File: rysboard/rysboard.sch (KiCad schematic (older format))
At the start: 1 part, among them J1 Raspberry_Pi_2_3

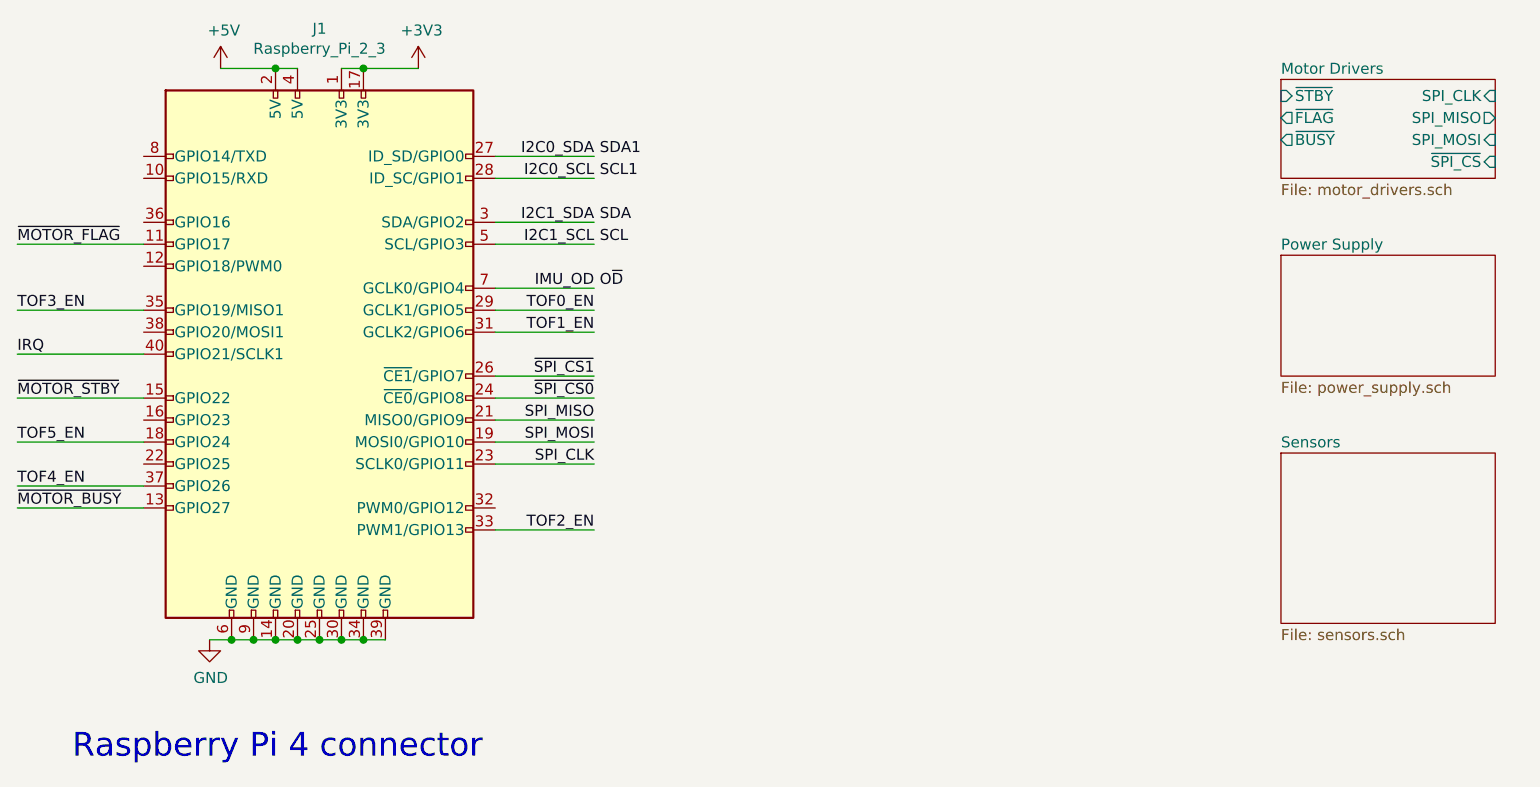
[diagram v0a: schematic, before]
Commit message: rysboard: schematic cleanup done after kicad import
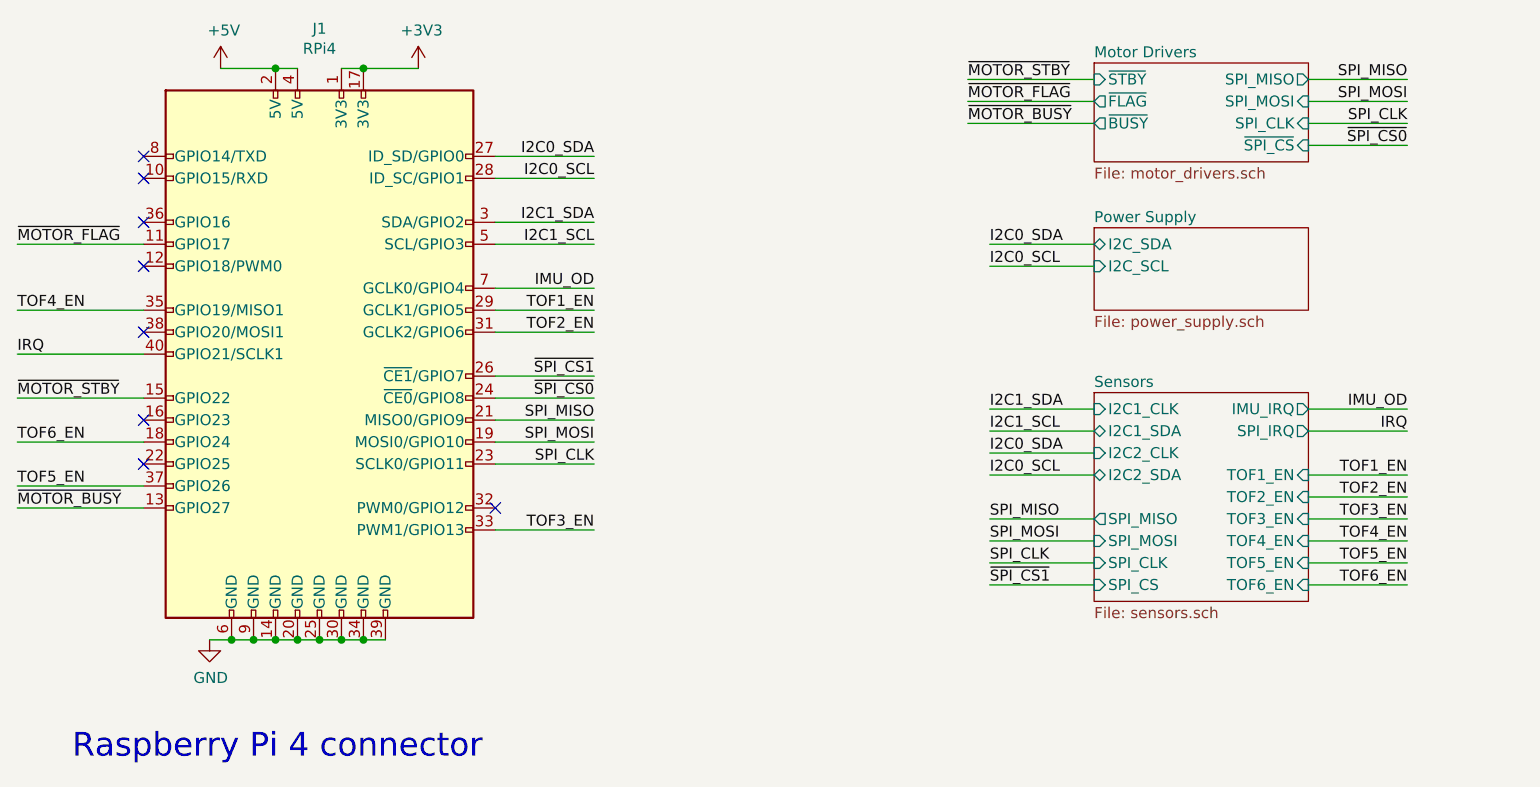
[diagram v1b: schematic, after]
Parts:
- J1: value Raspberry_Pi_2_3 -> RPi4; footprint (none) -> Connector_PinSocket_2.54mm:PinSocket_2x20_P2.54mm_Vertical
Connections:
- net TOF0_EN is gone; now on net TOF1_EN: J1.29 (GCLK1/GPIO5)
- net TOF1_EN: no longer J1.31 (GCLK2/GPIO6)
- net TOF2_EN: now also J1.31 (GCLK2/GPIO6); no longer J1.33 (PWM1/GPIO13)
- net TOF3_EN: now also J1.33 (PWM1/GPIO13); no longer J1.35 (GPIO19/MISO1)
- net TOF4_EN: now also J1.35 (GPIO19/MISO1); no longer J1.37 (GPIO26)
- net TOF5_EN: now also J1.37 (GPIO26); no longer J1.18 (GPIO24)
- new net TOF6_EN: J1.18 (GPIO24)
- no-connect marks 0 -> 8
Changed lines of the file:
@@
 Comment4 ""
 $EndDescr
-Text Label 4750 3025 0    50   ~ 0
-O~D~
-Text Label 4750 2525 0    50   ~ 0
-SCL1
-Text Label 4750 2425 0    50   ~ 0
-SDA1
 Text Notes 2350 5175 0    108  ~ 0
 Raspberry Pi 4 connector
-Text Label 4750 2825 0    50   ~ 0
-SCL
-Text Label 4750 2725 0    50   ~ 0
-SDA
 $Sheet
-S 7850 2075 975  450
+S 7000 2000 975  450
 U 5EB7428E
 F0 "Motor Drivers" 50
 F1 "motor_drivers.sch" 50
-F2 "~STBY" I L 7850 2150 50
-F3 "~FLAG" O L 7850 2250 50
-F4 "~BUSY" O L 7850 2350 50
-F5 "~SPI_CS" I R 8825 2450 50
-F6 "SPI_CLK" I R 8825 2150 50
-F7 "SPI_MISO" O R 8825 2250 50
-F8 "SPI_MOSI" I R 8825 2350 50
+F2 "~STBY" I L 7000 2075 50
+F3 "~FLAG" O L 7000 2175 50
+F4 "~BUSY" O L 7000 2275 50
+F5 "~SPI_CS" I R 7975 2375 50
+F6 "SPI_CLK" I R 7975 2275 50
+F7 "SPI_MISO" O R 7975 2075 50
+F8 "SPI_MOSI" I R 7975 2175 50
 $EndSheet
 $Sheet
-S 7850 2875 975  550
+S 7000 2750 975  375
 U 5E8FCBC6
 F0 "Power Supply" 50
 F1 "power_supply.sch" 50
+F2 "I2C_SDA" B L 7000 2825 50
+F3 "I2C_SCL" I L 7000 2925 50
 $EndSheet
 $Comp
@@
 P 3475 3325
 F 0 "J1" H 3475 4806 50  0000 C CNN
-F 1 "Raspberry_Pi_2_3" H 3475 4715 50  0000 C CNN
-F 2 "" H 3475 3325 50  0001 C CNN
+F 1 "RPi4" H 3475 4715 50  0000 C CNN
+F 2 "Connector_PinSocket_2.54mm:PinSocket_2x20_P2.54mm_Vertical" H 3475 3325 50  0001 C CNN
 F 3 "https://www.raspberrypi.org/documentation/hardware/raspberrypi/schematics/rpi_SCH_3bplus_1p0_reduced.pdf" H 3475 3325 50  0001 C CNN
 	1    3475 3325
@@
 $EndComp
 $Comp
-L power:+5V #PWR?
+L power:+5V #PWR02
 U 1 1 5EB8A55F
 P 3025 2025
-F 0 "#PWR?" H 3025 1875 50  0001 C CNN
+F 0 "#PWR02" H 3025 1875 50  0001 C CNN
 F 1 "+5V" H 3040 2198 50  0000 C CNN
 F 2 "" H 3025 2025 50  0001 C CNN
@@
 Connection ~ 3275 2025
 $Comp
-L power:+3V3 #PWR?
+L power:+3V3 #PWR03
 U 1 1 5EB8D8B6
 P 3925 2025
-F 0 "#PWR?" H 3925 1875 50  0001 C CNN
+F 0 "#PWR03" H 3925 1875 50  0001 C CNN
 F 1 "+3V3" H 3940 2198 50  0000 C CNN
 F 2 "" H 3925 2025 50  0001 C CNN
@@
 Connection ~ 3675 2025
 $Comp
-L power:GND #PWR?
+L power:GND #PWR01
 U 1 1 5EB9309D
 P 2975 4625
-F 0 "#PWR?" H 2975 4375 50  0001 C CNN
+F 0 "#PWR01" H 2975 4375 50  0001 C CNN
 F 1 "GND" H 2980 4452 50  0000 C CNN
 F 2 "" H 2975 4625 50  0001 C CNN
@@
 ~MOTOR_BUSY
 $Sheet
-S 7850 3775 975  775
+S 7000 3500 975  950
 U 5EA6D11C
 F0 "Sensors" 50
 F1 "sensors.sch" 50
+F2 "TOF6_EN" I R 7975 4375 50
+F3 "TOF5_EN" I R 7975 4275 50
+F4 "TOF4_EN" I R 7975 4175 50
+F5 "TOF2_EN" I R 7975 3975 50
+F6 "TOF1_EN" I R 7975 3875 50
+F7 "I2C1_CLK" I L 7000 3575 50
+F8 "I2C1_SDA" B L 7000 3675 50
+F9 "TOF3_EN" I R 7975 4075 50
+F10 "SPI_MOSI" I L 7000 4175 50
+F11 "SPI_MISO" O L 7000 4075 50
+F12 "SPI_CLK" I L 7000 4275 50
+F13 "SPI_CS" I L 7000 4375 50
+F14 "SPI_IRQ" O R 7975 3675 50
+F15 "I2C2_CLK" I L 7000 3775 50
+F16 "I2C2_SDA" B L 7000 3875 50
+F17 "IMU_IRQ" O R 7975 3575 50
 $EndSheet
 Wire Wire Line
@@
 	2675 3925 2100 3925
 Text Label 4725 3125 2    50   ~ 0
-TOF0_EN
+TOF1_EN
 Text Label 4725 3225 2    50   ~ 0
-TOF1_EN
+TOF2_EN
 Text Label 4725 4125 2    50   ~ 0
-TOF2_EN
+TOF3_EN
 Text Label 2100 3125 0    50   ~ 0
-TOF3_EN
+TOF4_EN
 Text Label 2100 3925 0    50   ~ 0
-TOF4_EN
+TOF5_EN
 Wire Wire Line
 	2675 3725 2100 3725
 Text Label 2100 3725 0    50   ~ 0
+TOF6_EN
+Wire Wire Line
+	7000 2175 6425 2175
+Text Label 6425 2175 0    50   ~ 0
+~MOTOR_FLAG
+Wire Wire Line
+	7000 2075 6425 2075
+Text Label 6425 2075 0    50   ~ 0
+~MOTOR_STBY
+Wire Wire Line
+	7000 2275 6425 2275
+Text Label 6425 2275 0    50   ~ 0
+~MOTOR_BUSY
+Wire Wire Line
+	7975 2075 8425 2075
+Text Label 8425 2075 2    50   ~ 0
+SPI_MISO
+Wire Wire Line
+	7975 2175 8425 2175
+Text Label 8425 2175 2    50   ~ 0
+SPI_MOSI
+Wire Wire Line
+	7975 2275 8425 2275
+Text Label 8425 2275 2    50   ~ 0
+SPI_CLK
+Wire Wire Line
+	7975 2375 8425 2375
+Text Label 8425 2375 2    50   ~ 0
+~SPI_CS0
+Text Label 6525 4075 0    50   ~ 0
+SPI_MISO
+Text Label 6525 4175 0    50   ~ 0
+SPI_MOSI
+Text Label 6525 4275 0    50   ~ 0
+SPI_CLK
+Text Label 6525 4375 0    50   ~ 0
+~SPI_CS1
+Wire Wire Line
+	7000 4075 6525 4075
+Wire Wire Line
+	6525 4175 7000 4175
+Wire Wire Line
+	7000 4275 6525 4275
+Wire Wire Line
+	6525 4375 7000 4375
+Text Label 6525 3875 0    50   ~ 0
+I2C0_SCL
+Text Label 6525 3775 0    50   ~ 0
+I2C0_SDA
+Text Label 6525 3575 0    50   ~ 0
+I2C1_SDA
+Text Label 6525 3675 0    50   ~ 0
+I2C1_SCL
+Wire Wire Line
+	7000 3575 6525 3575
+Wire Wire Line
+	6525 3675 7000 3675
+Wire Wire Line
+	7000 3775 6525 3775
+Wire Wire Line
+	6525 3875 7000 3875
+Text Label 6525 2925 0    50   ~ 0
+I2C0_SCL
+Text Label 6525 2825 0    50   ~ 0
+I2C0_SDA
+Wire Wire Line
+	7000 2825 6525 2825
+Wire Wire Line
+	6525 2925 7000 2925
+Wire Wire Line
+	7975 3875 8425 3875
+Wire Wire Line
+	7975 3975 8425 3975
+Text Label 8425 3875 2    50   ~ 0
+TOF1_EN
+Text Label 8425 3975 2    50   ~ 0
+TOF2_EN
+Wire Wire Line
+	7975 3575 8425 3575
+Text Label 8425 3575 2    50   ~ 0
+IMU_OD
+Text Label 8425 3675 2    50   ~ 0
+IRQ
+Wire Wire Line
+	7975 3675 8425 3675
+Wire Wire Line
+	7975 4075 8425 4075
+Text Label 8425 4075 2    50   ~ 0
+TOF3_EN
+Text Label 8425 4175 2    50   ~ 0
+TOF4_EN
+Text Label 8425 4275 2    50   ~ 0
 TOF5_EN
+Text Label 8425 4375 2    50   ~ 0
+TOF6_EN
+Wire Wire Line
+	7975 4175 8425 4175
+Wire Wire Line
+	7975 4275 8425 4275
+Wire Wire Line
+	7975 4375 8425 4375
+NoConn ~ 2675 2425
+NoConn ~ 2675 2525
+NoConn ~ 2675 2725
+NoConn ~ 2675 2925
+NoConn ~ 4275 4025
+NoConn ~ 2675 3825
+NoConn ~ 2675 3625
+NoConn ~ 2675 3225
 $EndSCHEMATC

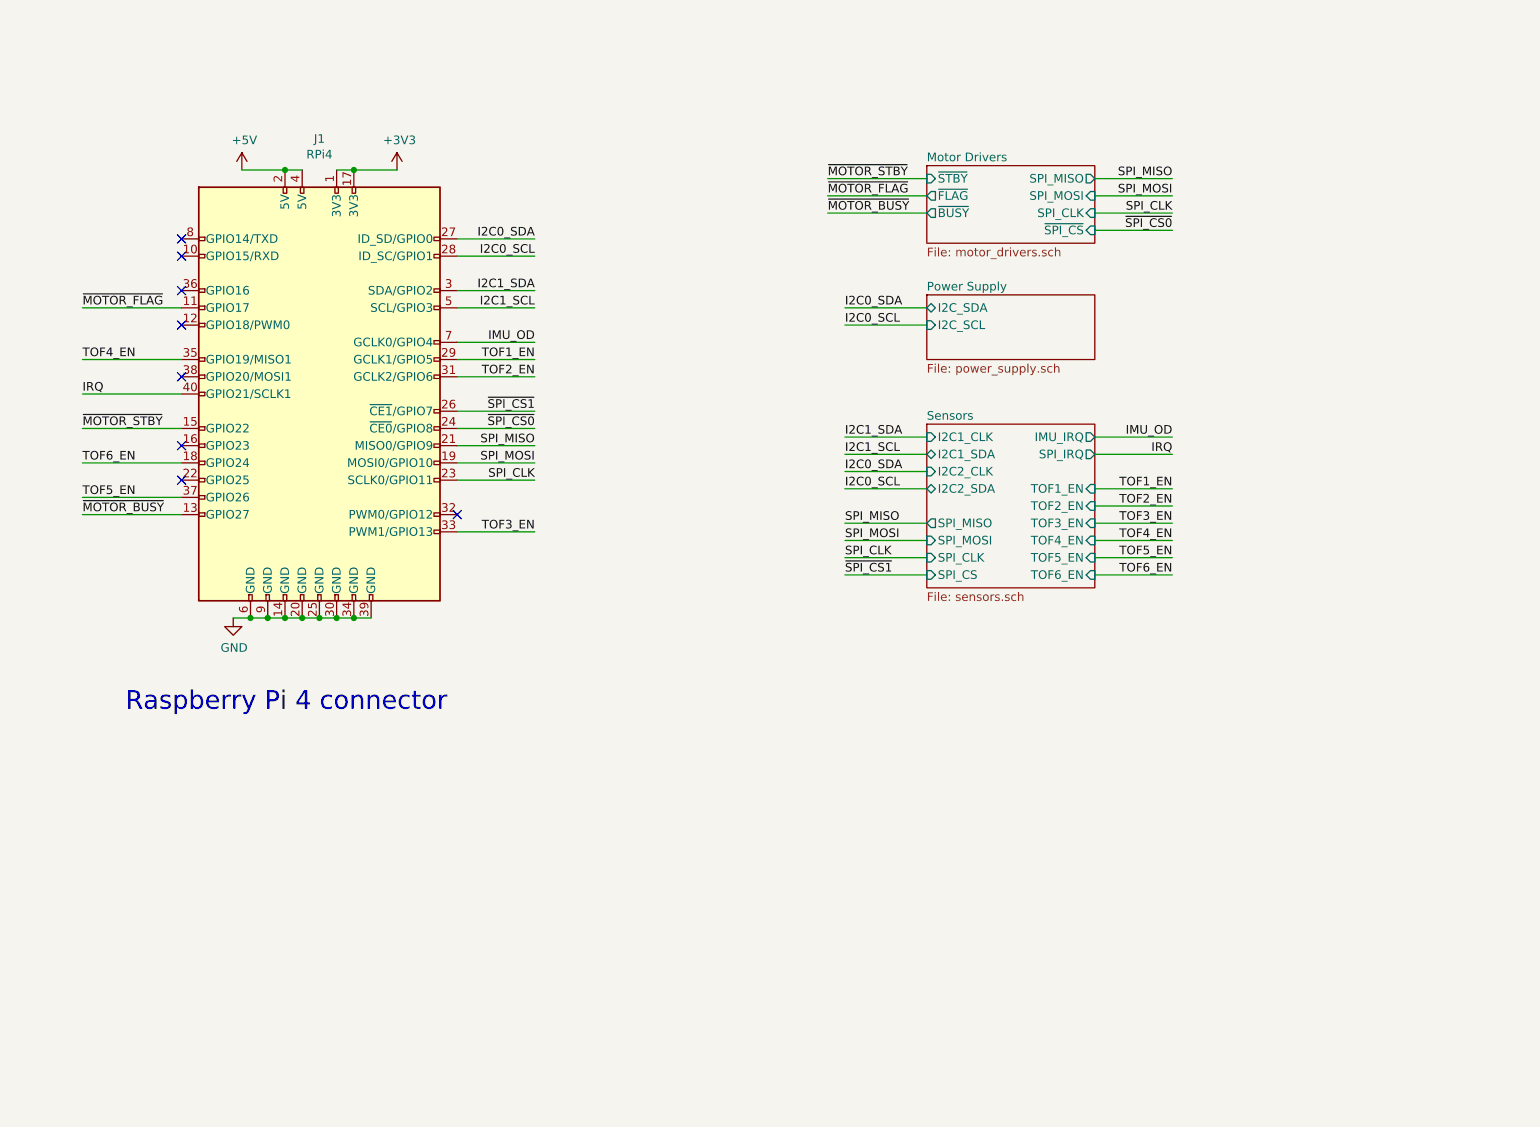
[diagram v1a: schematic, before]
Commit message: rysboard: 4.2 schematic
Change the I2C buses and GPIOs used
Fix L6470 connections
Change ADC to 4-channel
Add 2 user LEDs
Add I2C pullups
Add serial connector
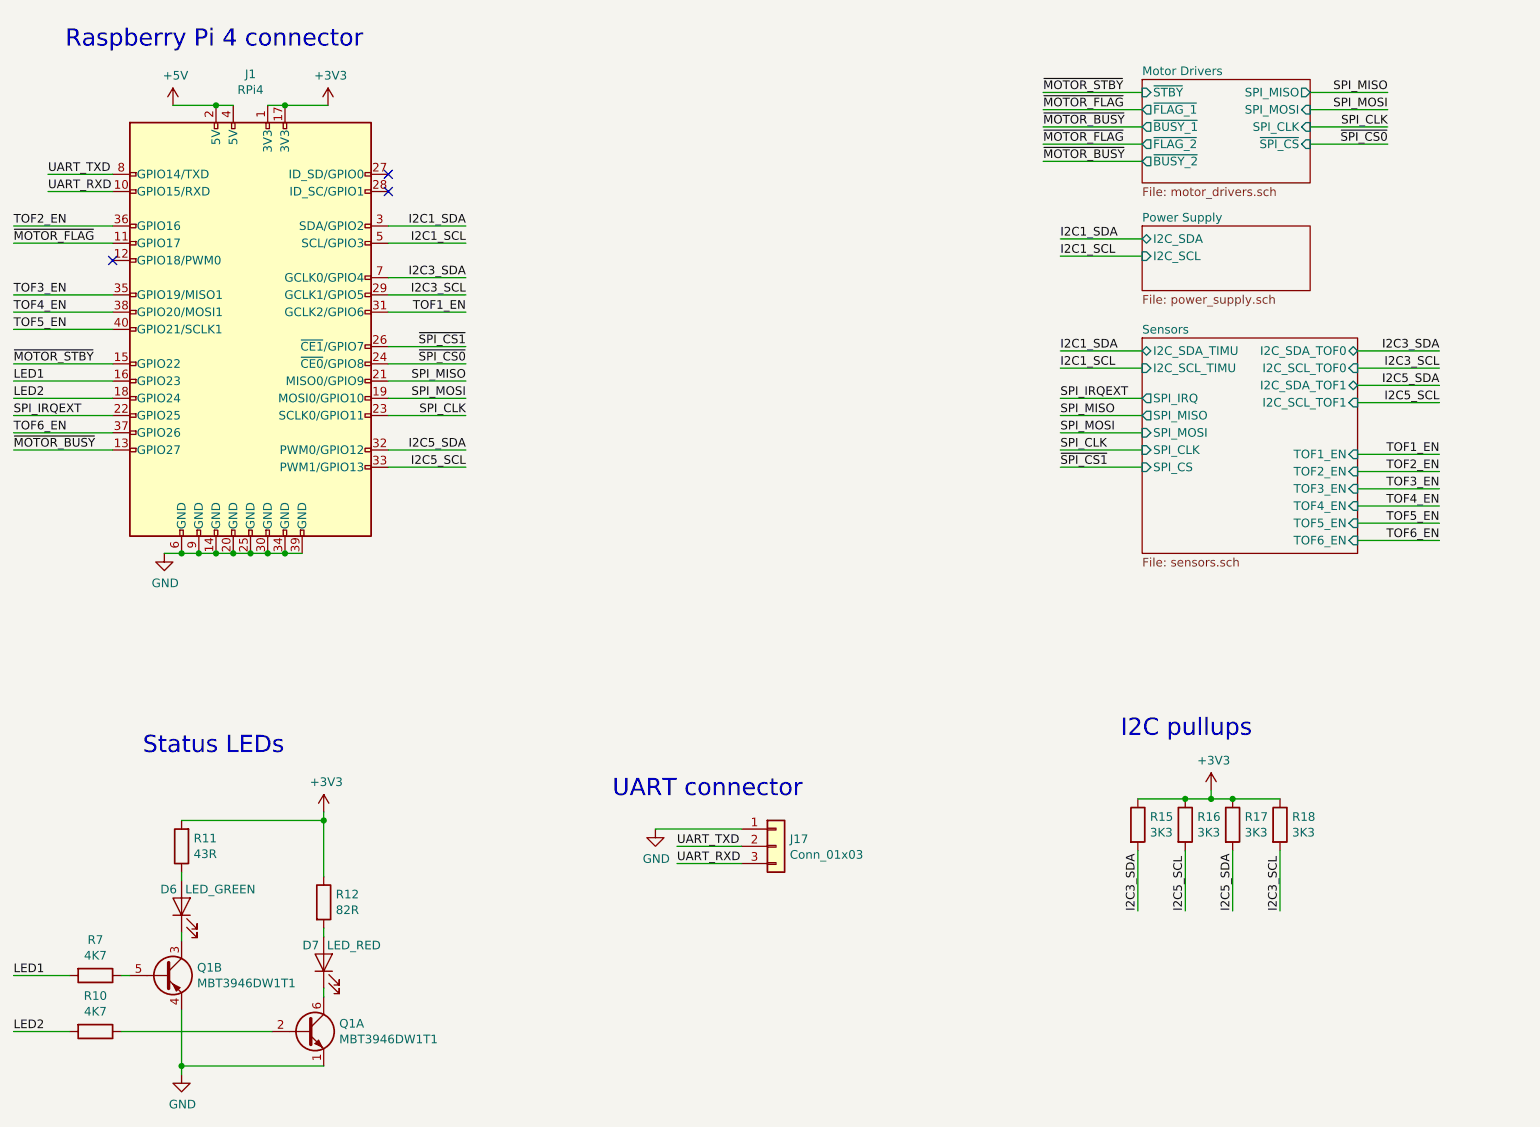
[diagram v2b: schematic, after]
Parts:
- added D6: LED_GREEN, LED_SMD:LED_0805_2012Metric, symbol Device:LED
- added D7: LED_RED, LED_SMD:LED_0805_2012Metric, symbol Device:LED
- added J17: Conn_01x03, Connector_PinHeader_2.54mm:PinHeader_1x03_P2.54mm_Vertical, symbol Connector_Generic:Conn_01x03
- added Q1: MBT3946DW1T1, Package_TO_SOT_SMD:SOT-363_SC-70-6, symbol Transistor_BJT:MBT3946DW1T1
- added R10, R7: 4K7, Resistor_SMD:R_0603_1608Metric, symbol Device:R
- added R11: 43R, Resistor_SMD:R_0603_1608Metric, symbol Device:R
- added R12: 82R, Resistor_SMD:R_0603_1608Metric, symbol Device:R
- added R15, R16, R17, R18: 3K3, Resistor_SMD:R_0603_1608Metric, symbol Device:R
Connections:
- net IRQ is gone; now on net TOF5_EN: J1.40 (GPIO21/SCLK1)
- net +3V3: now also R11.2, R12.1, R15.1, R16.1, R17.1, R18.1
- net GND: now also J17.1 (Pin_1), Q1.1 (E1), Q1.4 (E2)
- net TOF1_EN: now also J1.31 (GCLK2/GPIO6); no longer J1.29 (GCLK1/GPIO5)
- net TOF2_EN: now also J1.36 (GPIO16); no longer J1.31 (GCLK2/GPIO6)
- net TOF3_EN: now also J1.35 (GPIO19/MISO1); no longer J1.33 (PWM1/GPIO13)
- net TOF4_EN: now also J1.38 (GPIO20/MOSI1); no longer J1.35 (GPIO19/MISO1)
- net TOF5_EN: no longer J1.37 (GPIO26)
- net TOF6_EN: now also J1.37 (GPIO26); no longer J1.18 (GPIO24)
- net UART_RXD: now reaches J1.10 (GPIO15/RXD)
- net UART_RXD: now also J17.3 (Pin_3)
- net LED1: now reaches J1.16 (GPIO23)
- net LED1: now also R7.2
- net SPI_IRQEXT: now reaches J1.22 (GPIO25)
- net I2C5_SDA: now reaches J1.32 (PWM0/GPIO12)
- net I2C5_SDA: now also R17.2
- net UART_TXD: now reaches J1.8 (GPIO14/TXD)
- net UART_TXD: now also J17.2 (Pin_2)
- net I2C0_SCL: no longer names the net of J1.28 (ID_SC/GPIO1)
- net I2C0_SDA: no longer names the net of J1.27 (ID_SD/GPIO0)
- net IMU_OD renamed I2C3_SDA
- net I2C3_SDA: now also R15.2
- new net: Q1.2 (B1), R10.1
- new net: D7.1 (K), Q1.6 (C1)
- new net: D6.1 (K), Q1.3 (C2)
- new net: Q1.5 (B2), R7.1
- new net: D7.2 (A), R12.2
- new net: D6.2 (A), R11.1
- new net I2C3_SCL: J1.29 (GCLK1/GPIO5), R18.2
- new net I2C5_SCL: J1.33 (PWM1/GPIO13), R16.2
- new net LED2: J1.18 (GPIO24), R10.2
- no-connect marks 8 -> 3
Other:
- note added: "I2C pullups"
- note added: "Status LEDs"
- note added: "UART connector"
- moved on the sheet: J1
